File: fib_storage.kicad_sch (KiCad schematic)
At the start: 1 part, among them J2 Bus_M.2_Socket_M

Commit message: added symbol&footprint for orin/sodimm, added a bunch of specs and docs, partially implemented audio, full steam ahead
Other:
- moved on the sheet: J2
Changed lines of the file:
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@@
 	(symbol
 		(lib_id "Connector:Bus_M.2_Socket_M")
-		(at 77.47 81.28 0)
+		(at 86.36 81.28 0)
 		(unit 1)
 		(exclude_from_sim no)
@@
 		(fields_autoplaced yes)
 		(property "Reference" "J2"
-			(at 79.6641 30.48 0)
+			(at 88.5541 30.48 0)
 			(effects
 				(font
@@
 		)
 		(property "Value" "Bus_M.2_Socket_M"
-			(at 79.6641 33.02 0)
+			(at 88.5541 33.02 0)
 			(effects
 				(font
@@
 		)
 		(property "Footprint" ""
-			(at 77.47 54.61 0)
+			(at 86.36 54.61 0)
 			(effects
 				(font
@@
 		)
 		(property "Datasheet" "http://read.pudn.com/downloads794/doc/project/3133918/PCIe_M.2_Electromechanical_Spec_Rev1.0_Final_11012013_RS_Clean.pdf#page=155"
-			(at 77.47 54.61 0)
+			(at 86.36 54.61 0)
 			(effects
 				(font
@@
 		)
 		(property "Description" "M.2 Socket 3 Mechanical Key M"
-			(at 77.47 81.28 0)
+			(at 86.36 81.28 0)
 			(effects
 				(font

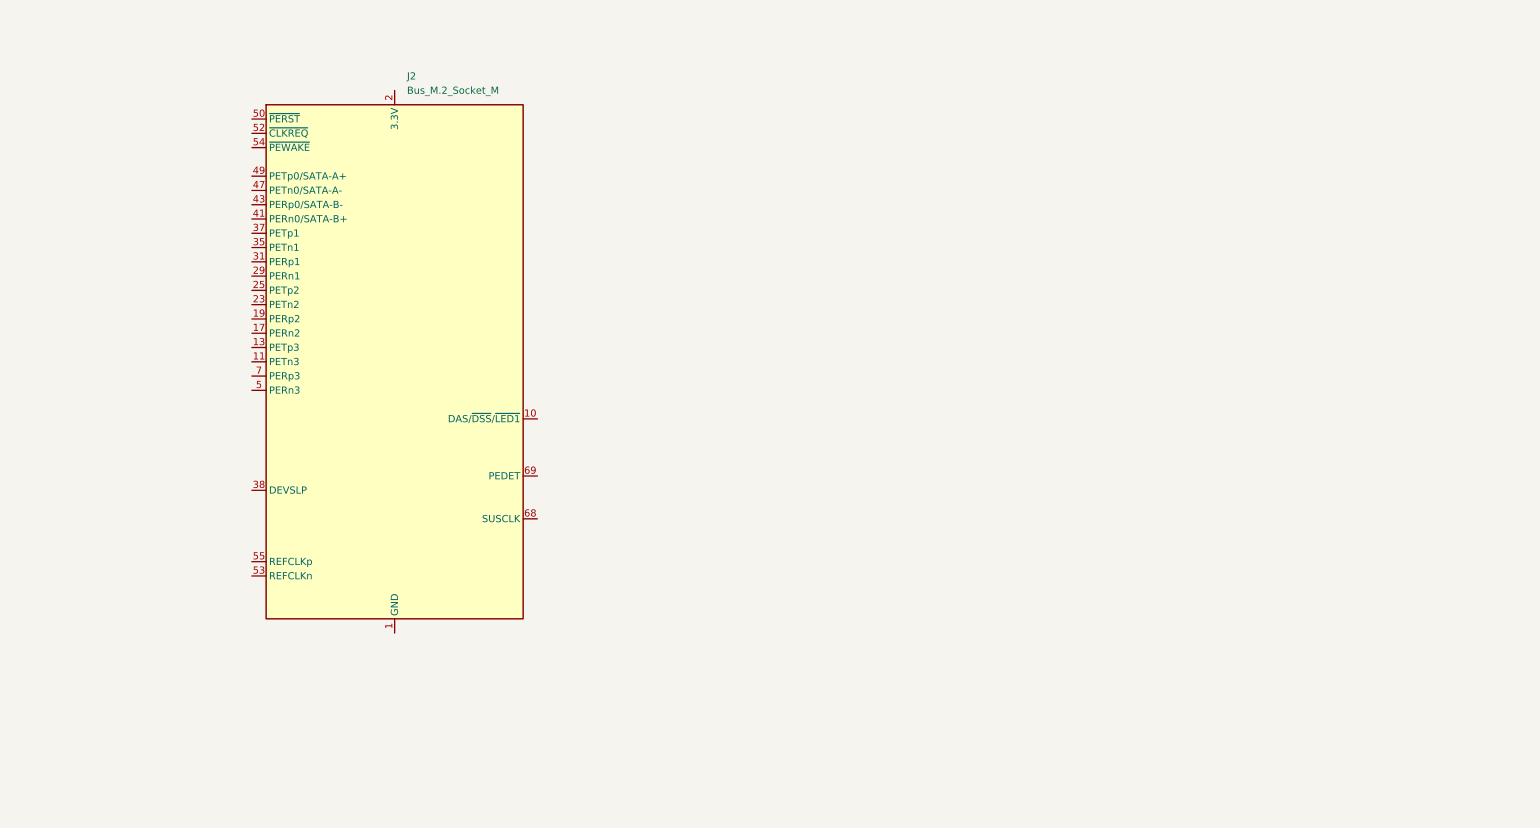
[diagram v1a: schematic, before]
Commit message: added usb+PD+DP & pcie implementations from antmicro design, added specs for USB components, rethought power+usb arch
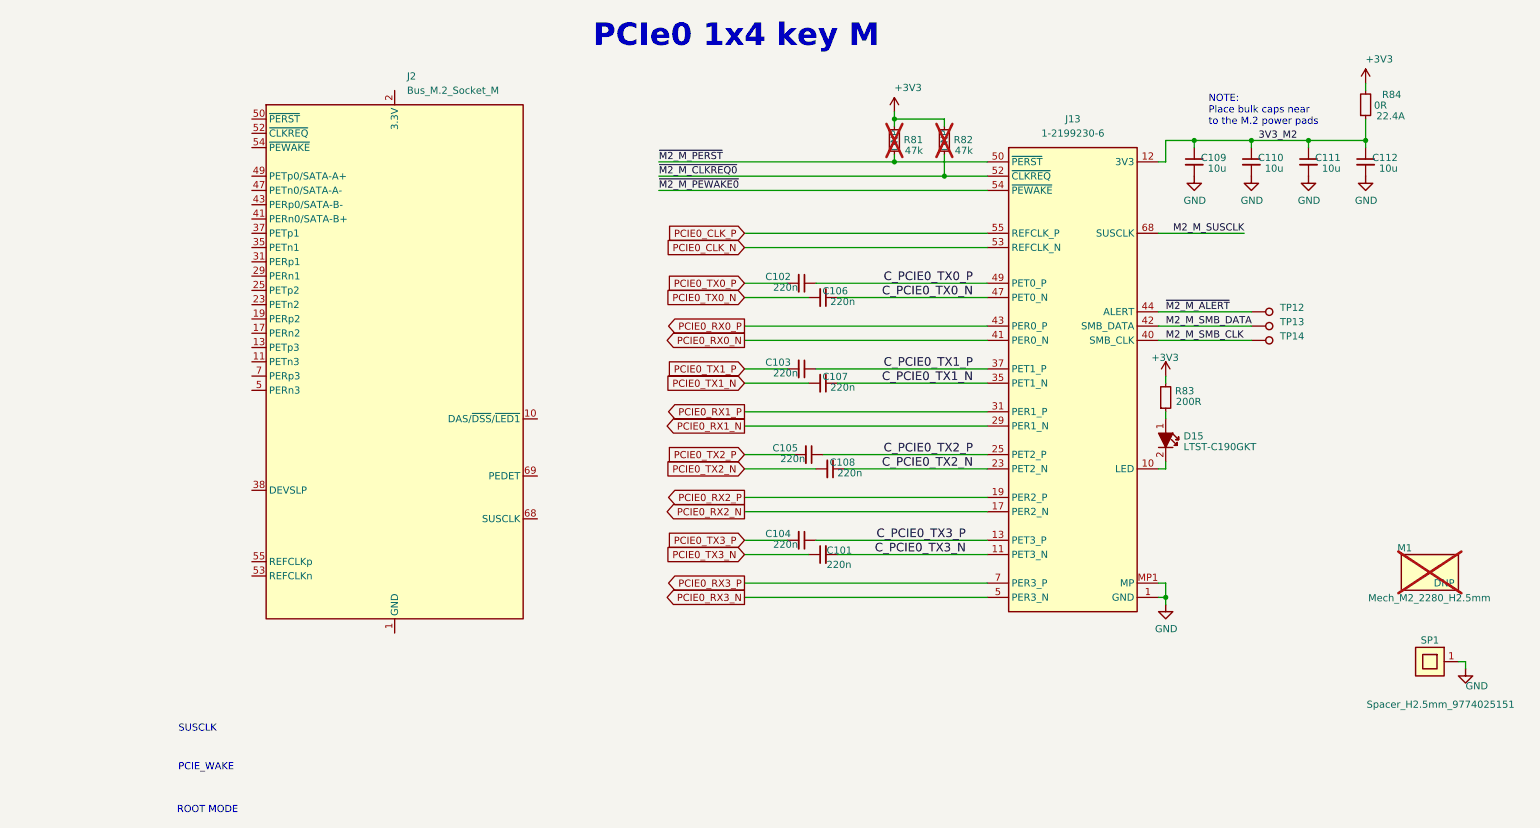
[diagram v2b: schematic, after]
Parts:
- added C101, C102, C103, C104, C105, C106, C107, C108: C_220n_0402, jetson-orin-baseboard-footprints:C_0402_1005Metric, symbol jetson-orin-baseboard:C_220n_0402
- added C109, C110, C111, C112: C_10u_0603, jetson-orin-baseboard-footprints:C_0603_1608Metric, symbol jetson-orin-baseboard:C_10u_0603
- added D15: LED_G_0603_LTST-C190GKT, jetson-orin-baseboard-footprints:LED_0603_1608Metric_G, symbol jetson-orin-baseboard:LED_G_0603_LTST-C190GKT
- added J13: Bus_M.2_1-2199230-6, jetson-orin-baseboard-footprints:Bus_M.2_Socket_Key_M_TE_1-2199230-6, symbol jetson-orin-baseboard:Bus_M.2_1-2199230-6
- added M1: Mech_M2_2280_H2.5mm, jetson-orin-baseboard-footprints:Mech_M2_2280_H2.5mm, symbol jetson-orin-baseboard:Mech_M2_2280_H2.5mm
- added R81, R82: R_47k_0402, jetson-orin-baseboard-footprints:R_0402_1005Metric, symbol jetson-orin-baseboard:R_47k_0402
- added R83: R_200R_0402, jetson-orin-baseboard-footprints:R_0402_1005Metric, symbol jetson-orin-baseboard:R_200R_0402
- added R84: R_0R_22.4A_0603, jetson-orin-baseboard-footprints:R_0603_1608Metric, symbol jetson-orin-baseboard:R_0R_22.4A_0603
- added SP1: Spacer_H2.5mm_9774025151, jetson-orin-baseboard-footprints:Spacer_Drill3.7mm_H2.5mm_9774025151R, symbol jetson-orin-baseboard:Spacer_Drill3.7mm_H2.5mm_9774025151R
- added TP12, TP13, TP14: TP_0.75mm_SMD, jetson-orin-baseboard-footprints:TP_SMD_0.75mm, symbol jetson-orin-baseboard:TP_0.75mm_SMD
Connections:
- new net: D15.2, J13.10 (LED)
- new net: D15.1, R83.1
- new net +3V3: R81.1, R82.1, R83.2, R84.2
- new net 3V3_M2: C109.1, C110.1, C111.1, C112.1, J13.12 (3V3), J13.14 (3V3), J13.16 (3V3), J13.18 (3V3), J13.2 (3V3), J13.4 (3V3), J13.70 (3V3), J13.72 (3V3), J13.74 (3V3), R84.1
- new net C_PCIE0_TX0_N: C106.1, J13.47 (PET0_N)
- new net C_PCIE0_TX0_P: C102.1, J13.49 (PET0_P)
- new net C_PCIE0_TX1_N: C107.1, J13.35 (PET1_N)
- new net C_PCIE0_TX1_P: C103.1, J13.37 (PET1_P)
- new net C_PCIE0_TX2_N: C108.1, J13.23 (PET2_N)
- new net C_PCIE0_TX2_P: C105.1, J13.25 (PET2_P)
- new net C_PCIE0_TX3_N: C101.2, J13.11 (PET3_N)
- new net C_PCIE0_TX3_P: C104.1, J13.13 (PET3_P)
- new net GND: C109.2, C110.2, C111.2, C112.2, J13.1 (GND), J13.15 (GND), J13.21 (GND), J13.27 (GND), J13.3 (GND), J13.33 (GND), J13.39 (GND), J13.45 (GND), J13.51 (GND), J13.57 (GND), J13.71 (GND), J13.73 (GND), J13.75 (GND), J13.9 (GND), J13.MP1 (MP), J13.MP2 (MP), SP1.1
- new net M2_M_SMB_CLK: J13.40 (SMB_CLK), TP14.1
- new net M2_M_SMB_DATA: J13.42 (SMB_DATA), TP13.1
- new net M2_M_SUSCLK: J13.68 (SUSCLK)
- new net PCIE0_CLK_N: J13.53 (REFCLK_N)
- new net PCIE0_CLK_P: J13.55 (REFCLK_P)
- new net PCIE0_RX0_N: J13.41 (PER0_N)
- new net PCIE0_RX0_P: J13.43 (PER0_P)
- new net PCIE0_RX1_N: J13.29 (PER1_N)
- new net PCIE0_RX1_P: J13.31 (PER1_P)
- new net PCIE0_RX2_N: J13.17 (PER2_N)
- new net PCIE0_RX2_P: J13.19 (PER2_P)
- new net PCIE0_RX3_N: J13.5 (PER3_N)
- new net PCIE0_RX3_P: J13.7 (PER3_P)
- new net PCIE0_TX0_N: C106.2
- new net PCIE0_TX0_P: C102.2
- new net PCIE0_TX1_N: C107.2
- new net PCIE0_TX1_P: C103.2
- new net PCIE0_TX2_N: C108.2
- new net PCIE0_TX2_P: C105.2
- new net PCIE0_TX3_N: C101.1
- new net PCIE0_TX3_P: C104.2
- new net ~{M2_M_ALERT}: J13.44 (ALERT), TP12.1
- new net ~{M2_M_CLKREQ0}: J13.52 (~{CLKREQ}), R82.2
- new net ~{M2_M_PERST}: J13.50 (~{PERST}), R81.2
- new net ~{M2_M_PEWAKE0}: J13.54 (~{PEWAKE})
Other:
- note added: "NOTE: Place bulk caps near to the M.2 power pads"
- note added: "PCIE_WAKE"
- note added: "PCIe0 1x4 key M"
- note added: "ROOT MODE"
- note added: "SUSCLK"

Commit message: added nets for 40 pin headers (epd & rpi header) connected some of the nets i'm reeusing
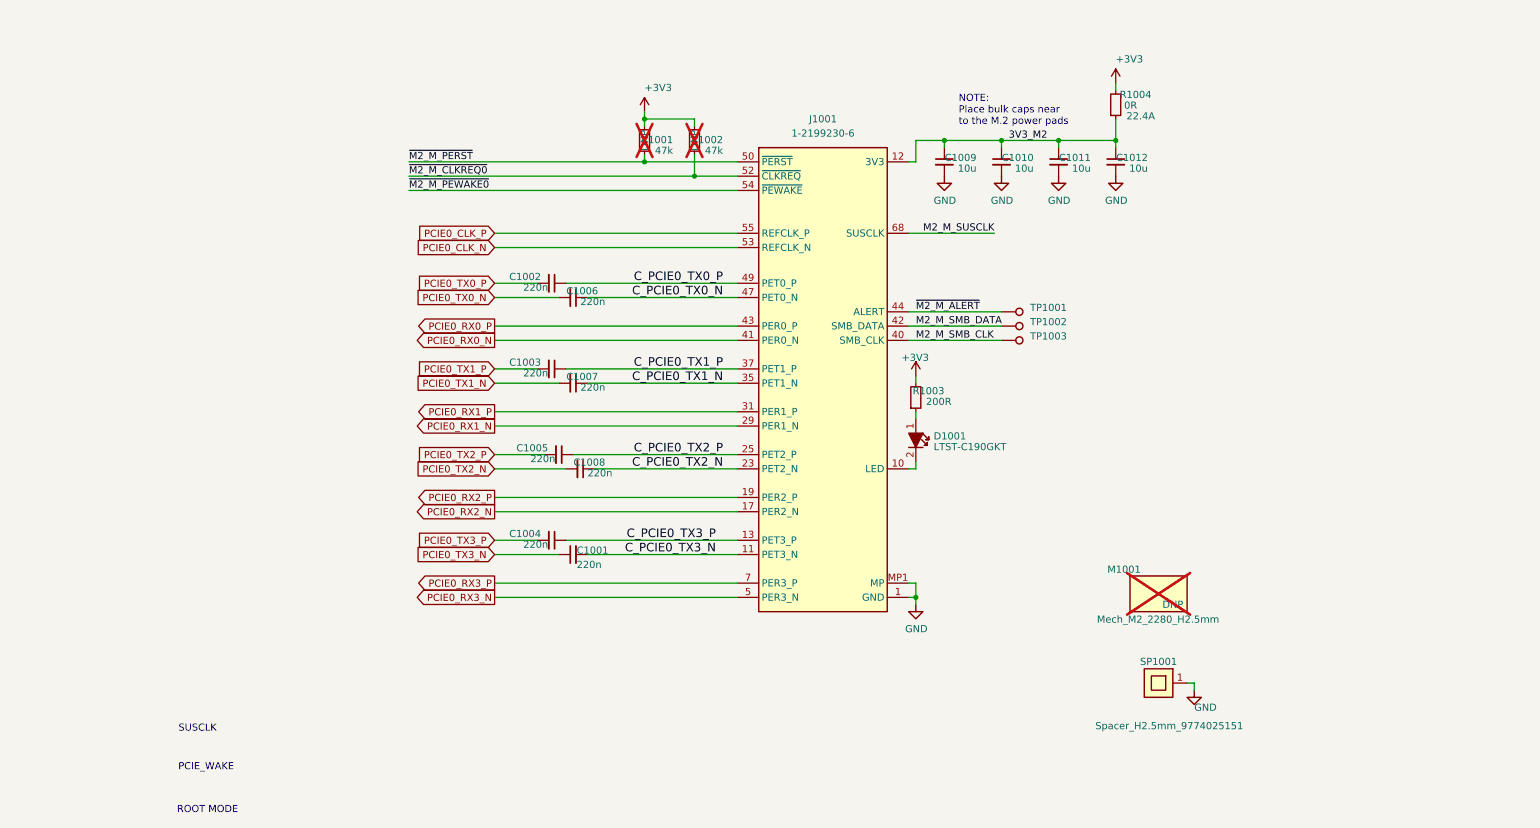
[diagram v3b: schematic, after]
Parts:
- removed J2: Bus_M.2_Socket_M, symbol Connector:Bus_M.2_Socket_M
- C1001: renamed from C101; value C_220n_0402 -> 220nF; footprint jetson-orin-baseboard-footprints:C_0402_1005Metric -> Capacitor_SMD:C_0603_1608Metric
- C1002: renamed from C102; value C_220n_0402 -> 220nF; footprint jetson-orin-baseboard-footprints:C_0402_1005Metric -> Capacitor_SMD:C_0603_1608Metric
- C1003: renamed from C103; value C_220n_0402 -> 220nF; footprint jetson-orin-baseboard-footprints:C_0402_1005Metric -> Capacitor_SMD:C_0603_1608Metric
- C1004: renamed from C104; value C_220n_0402 -> 220nF; footprint jetson-orin-baseboard-footprints:C_0402_1005Metric -> Capacitor_SMD:C_0603_1608Metric
- C1005: renamed from C105; value C_220n_0402 -> 220nF; footprint jetson-orin-baseboard-footprints:C_0402_1005Metric -> Capacitor_SMD:C_0603_1608Metric
- C1006: renamed from C106; value C_220n_0402 -> 220nF; footprint jetson-orin-baseboard-footprints:C_0402_1005Metric -> Capacitor_SMD:C_0603_1608Metric
- C1007: renamed from C107; value C_220n_0402 -> 220nF; footprint jetson-orin-baseboard-footprints:C_0402_1005Metric -> Capacitor_SMD:C_0603_1608Metric
- C1008: renamed from C108; value C_220n_0402 -> 220nF; footprint jetson-orin-baseboard-footprints:C_0402_1005Metric -> Capacitor_SMD:C_0603_1608Metric
- C1009: renamed from C109; value C_10u_0603 -> 20uF; footprint jetson-orin-baseboard-footprints:C_0603_1608Metric -> Capacitor_SMD:C_0603_1608Metric
- C1010: renamed from C110; value C_10u_0603 -> 20uF; footprint jetson-orin-baseboard-footprints:C_0603_1608Metric -> Capacitor_SMD:C_0603_1608Metric
- C1011: renamed from C111; value C_10u_0603 -> 20uF; footprint jetson-orin-baseboard-footprints:C_0603_1608Metric -> Capacitor_SMD:C_0603_1608Metric
- C1012: renamed from C112; value C_10u_0603 -> 20uF; footprint jetson-orin-baseboard-footprints:C_0603_1608Metric -> Capacitor_SMD:C_0603_1608Metric
- R1001: renamed from R81; value R_47k_0402 -> 47K; footprint jetson-orin-baseboard-footprints:R_0402_1005Metric -> Resistor_SMD:R_0603_1608Metric
- R1002: renamed from R82; value R_47k_0402 -> 47K; footprint jetson-orin-baseboard-footprints:R_0402_1005Metric -> Resistor_SMD:R_0603_1608Metric
- R1003: renamed from R83; value R_200R_0402 -> 200R; footprint jetson-orin-baseboard-footprints:R_0402_1005Metric -> Resistor_SMD:R_0603_1608Metric
- R1004: renamed from R84; value R_0R_22.4A_0603 -> 0R 22A; footprint jetson-orin-baseboard-footprints:R_0603_1608Metric -> Resistor_SMD:R_0603_1608Metric
- TP1001: renamed from TP12; footprint jetson-orin-baseboard-footprints:TP_SMD_0.75mm -> TestPoint:TestPoint_Pad_D1.0mm
- TP1002: renamed from TP13; footprint jetson-orin-baseboard-footprints:TP_SMD_0.75mm -> TestPoint:TestPoint_Pad_D1.0mm
- TP1003: renamed from TP14; footprint jetson-orin-baseboard-footprints:TP_SMD_0.75mm -> TestPoint:TestPoint_Pad_D1.0mm
- renumbered D15 to D1001, J13 to J1001, M1 to M1001, SP1 to SP1001
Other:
- note removed: "PCIe0 1x4 key M"
- moved on the sheet: C1001, C1002, C1003, C1004, C1005, C1006, C1007, C1008, C1009, C1010, C1011, C1012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

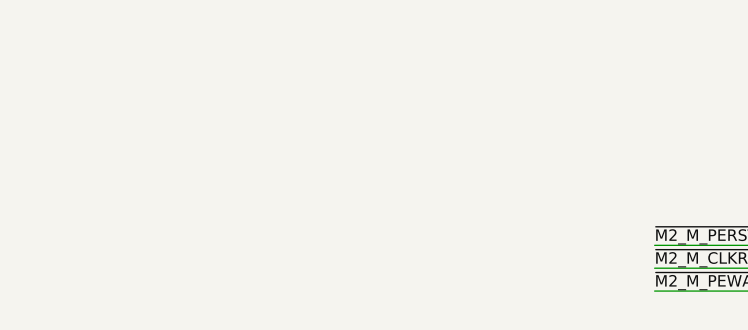
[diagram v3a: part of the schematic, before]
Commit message: continuing schematic work for pcie and other high speed interfaces
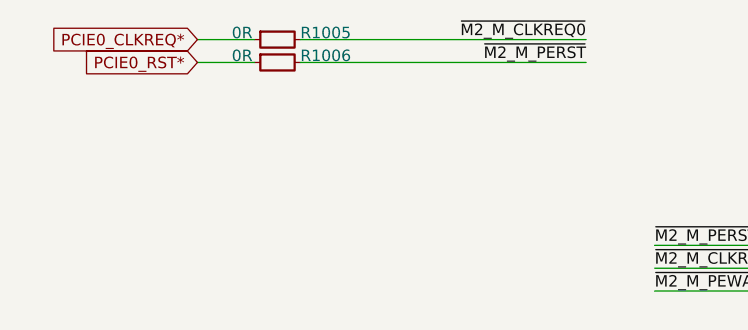
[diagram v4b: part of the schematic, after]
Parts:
- added R1005, R1006: R_0R_0402, jetson-orin-baseboard-footprints:R_0402_1005Metric, symbol jetson-orin-baseboard:R_0R_0402
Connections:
- net ~{M2_M_CLKREQ0}: now also R1005.2
- net ~{M2_M_PERST}: now also R1006.2
- new net PCIE0_CLKREQ*: R1005.1
- new net PCIE0_RST*: R1006.1

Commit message: refactored PCIe pages
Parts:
- removed C1001, C1002, C1003, C1004, C1005, C1006, C1007, C1008: 220nF, Capacitor_SMD:C_0603_1608Metric, symbol jetson-orin-baseboard:C_220n_0402
- removed C1009, C1010, C1011, C1012: 20uF, Capacitor_SMD:C_0603_1608Metric, symbol jetson-orin-baseboard:C_10u_0603
- removed D1001: LED_G_0603_LTST-C190GKT, jetson-orin-baseboard-footprints:LED_0603_1608Metric_G, symbol jetson-orin-baseboard:LED_G_0603_LTST-C190GKT
- removed J1001: Bus_M.2_1-2199230-6, jetson-orin-baseboard-footprints:Bus_M.2_Socket_Key_M_TE_1-2199230-6, symbol jetson-orin-baseboard:Bus_M.2_1-2199230-6
- removed M1001: Mech_M2_2280_H2.5mm, jetson-orin-baseboard-footprints:Mech_M2_2280_H2.5mm, symbol jetson-orin-baseboard:Mech_M2_2280_H2.5mm
- removed R1001, R1002: 47K, Resistor_SMD:R_0603_1608Metric, symbol jetson-orin-baseboard:R_47k_0402
- removed R1003: 200R, Resistor_SMD:R_0603_1608Metric, symbol jetson-orin-baseboard:R_200R_0402
- removed R1004: 0R 22A, Resistor_SMD:R_0603_1608Metric, symbol jetson-orin-baseboard:R_0R_22.4A_0603
- removed R1005, R1006: R_0R_0402, jetson-orin-baseboard-footprints:R_0402_1005Metric, symbol jetson-orin-baseboard:R_0R_0402
- removed SP1001: Spacer_H2.5mm_9774025151, jetson-orin-baseboard-footprints:Spacer_Drill3.7mm_H2.5mm_9774025151R, symbol jetson-orin-baseboard:Spacer_Drill3.7mm_H2.5mm_9774025151R
- removed TP1001, TP1002, TP1003: TP_0.75mm_SMD, TestPoint:TestPoint_Pad_D1.0mm, symbol jetson-orin-baseboard:TP_0.75mm_SMD
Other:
- note removed: "NOTE: Place bulk caps near to the M.2 power pads"
- note removed: "PCIE_WAKE"
- note removed: "ROOT MODE"
- note removed: "SUSCLK"
